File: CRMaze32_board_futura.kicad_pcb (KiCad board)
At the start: 2 copper layers, 74 x 100 mm, 70 parts, among them J101 CONN_01X02, J102 CONN_01X02, P101 GYRO_ADXRS_2, P102 GYRO_ADXRS_1, P103 SERIAL, P104 ENC_1_IN, P105 ENC_1_POWER, P106 ENC_2_IN, P107 ENC_2_POWER, P108 MOTOR1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

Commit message: retoques y moificaciones
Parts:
- removed P101: GYRO_ADXRS_2, Pin_Headers:Pin_Header_Straight_1x05
- added J103: GYRO_ADXRS_2, Pin_Headers:Pin_Header_Straight_1x06, F.Cu at (128.0, 55.5)
- moved C115 13.2 mm to (160.2, 67.7)
- moved C114 7.94 mm to (160.0, 65.2)
- moved C106 7.93 mm to (117.2, 60.9), turned to 270 degrees
- moved C105 4.42 mm to (114.5, 60.9), turned to 270 degrees
- moved 10ohm101 3.94 mm to (123.7, 53.9), turned to 50 degrees
- moved SW101 3.34 mm to (113.5, 72.5)
- moved D108 2.96 mm to (116.3, 56.7), turned to 50 degrees
- moved D106 2.56 mm to (155.0, 56.4), turned to 130 degrees
- moved 10uH101 2.51 mm to (128.5, 52.0)
- moved P107 2.33 mm to (157.0, 82.5)
- moved P104 2.27 mm to (113.5, 82.5)
- moved P102 1.97 mm to (133.6, 55.5)
- moved P105 1.90 mm to (113.5, 106.5), turned to 180 degrees
- moved 2.8ohm101 1.84 mm to (114.7, 65.3)
- moved D112 1.55 mm to (151.5, 52.1), turned to 130 degrees
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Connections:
- U101 pad 36: M1_DIR -> M1_EN
- U101 pad 37: M1_EN -> M1_DIR

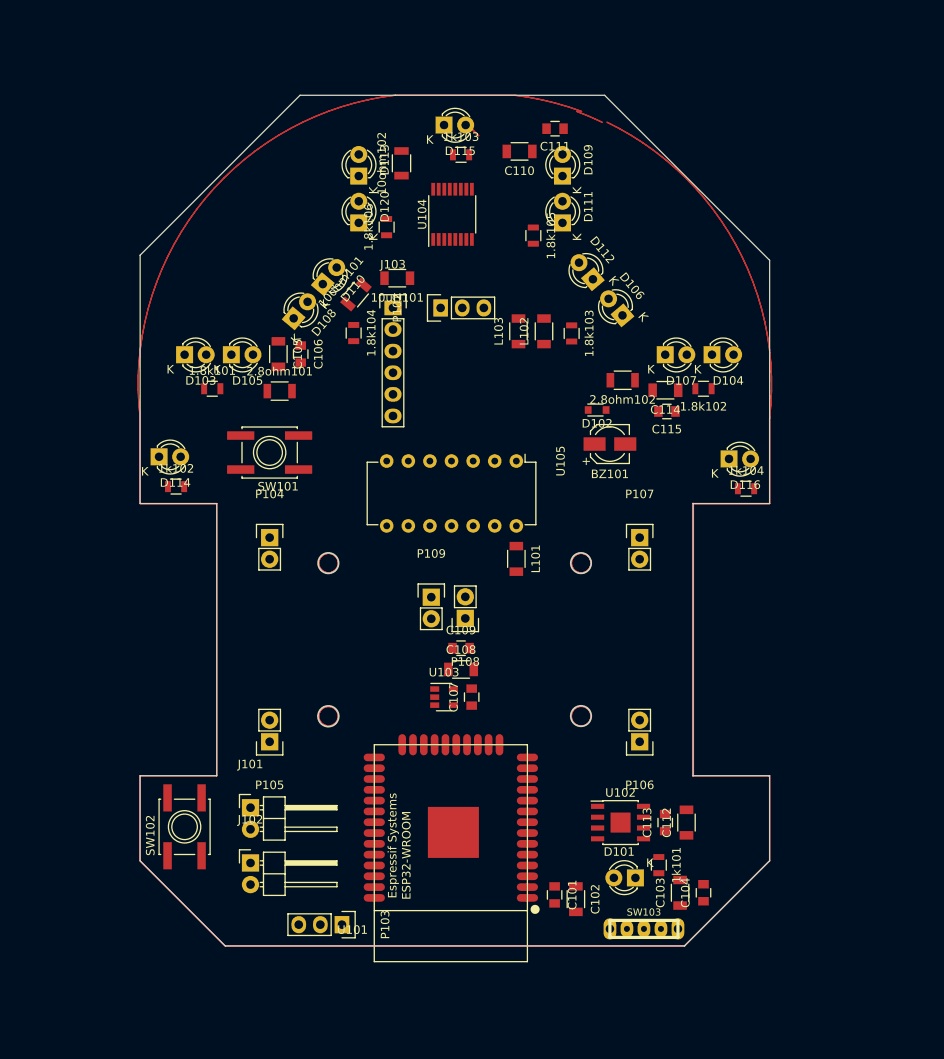
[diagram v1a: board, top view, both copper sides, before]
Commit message: esquematico finalizado. Componentes colocados. Comienzo del enrutado.
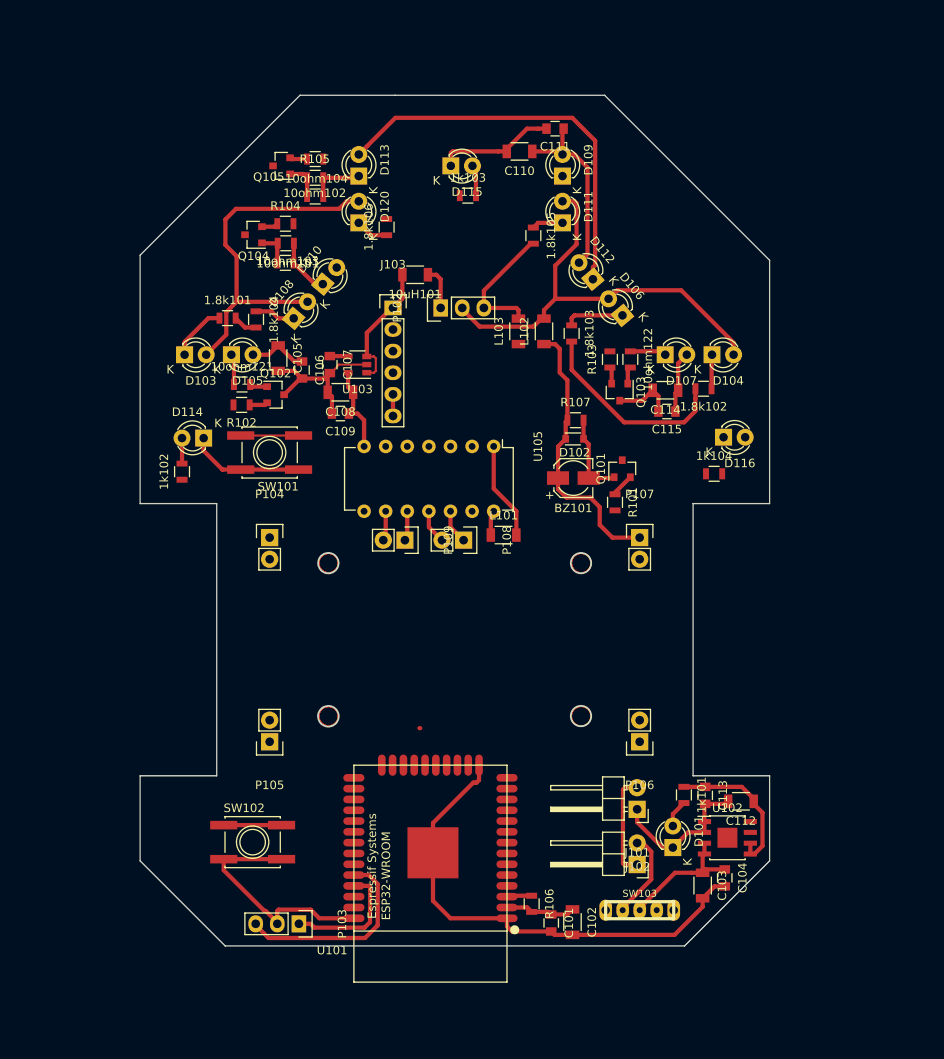
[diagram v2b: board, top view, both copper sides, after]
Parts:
- removed 2.8ohm101, 2.8ohm102: R, Resistors_SMD:R_1206
- removed U104: ULN2003A, Housings_SSOP:TSSOP-16_4.4x5mm_Pitch0.65mm
- added 10ohm103: R, Resistors_SMD:R_0805, F.Cu at (115.4, 47.9)
- added 10ohm104: R, Resistors_SMD:R_0805, F.Cu at (118.8, 40.2)
- added 10ohm121: R, Resistors_SMD:R_0805, F.Cu at (110.2, 64.5)
- added 10ohm122: R, Resistors_SMD:R_0805, F.Cu at (155.9, 61.5)
- added Q101: BS107, TO_SOT_Packages_SMD:SOT-23, F.Cu at (154.9, 74.4)
- added Q102: BS107, TO_SOT_Packages_SMD:SOT-23, F.Cu at (114.2, 65.7)
- added Q103: BS107, TO_SOT_Packages_SMD:SOT-23, F.Cu at (154.7, 65.4)
- added Q104: BS107, TO_SOT_Packages_SMD:SOT-23, F.Cu at (111.6, 46.9)
- added Q105: BS107, TO_SOT_Packages_SMD:SOT-23, F.Cu at (114.9, 38.8)
- added R101: R, Resistors_SMD:R_0805, F.Cu at (154.1, 78.3)
- added R102: R, Resistors_SMD:R_0805, F.Cu at (110.2, 66.9)
- added R103: R, Resistors_SMD:R_0805, F.Cu at (153.5, 61.5)
- added R104: R, Resistors_SMD:R_0805, F.Cu at (115.3, 45.6)
- added R105: R, Resistors_SMD:R_0805, F.Cu at (118.8, 38.0)
- added R106: R, Resistors_SMD:R_0805, F.Cu at (144.3, 125.5)
- added R107: R, Resistors_SMD:R_0805, F.Cu at (149.4, 68.7)
- 10ohm101, 10ohm102: footprint Resistors_SMD:R_1206 -> Resistors_SMD:R_0805
- moved J101 45.5 mm to (156.7, 114.4), turned to 180 degrees
- moved J102 45.5 mm to (156.7, 120.9), turned to 180 degrees
- moved C107 42.5 mm to (120.6, 62.2), turned to 270 degrees
- moved U103 40.4 mm to (123.8, 62.2), turned to 180 degrees
- moved C108 35.5 mm to (121.8, 65.4), turned to 180 degrees
- moved C109 31.0 mm to (121.8, 67.9), turned to 180 degrees
- moved U102 12.7 mm to (167.3, 117.8)
- moved 1.8k104 11.6 mm to (111.9, 56.9)
- moved 10ohm102 10.9 mm to (118.8, 42.4), turned to 180 degrees
- moved P108 9.20 mm to (136.3, 82.8), turned to 270 degrees
- moved 10ohm101 9.10 mm to (115.3, 50.2), turned to 180 degrees
- moved 1k101 8.76 mm to (162.2, 112.8)
- moved 1.8k101 8.49 mm to (108.5, 56.7)
- moved SW102 8.20 mm to (111.5, 118.3), turned to 0 degrees
- moved P109 7.38 mm to (129.4, 82.8), turned to 270 degrees
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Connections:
- net BUZZER_CONTROL renamed Net-(BZ101-Pad2)
- C104 pad 2: (no net) -> GND
- U101 pad 14: ENC_2_B -> M1_DIR
- U101 pad 29: GPIO_IR_SIDE -> M2_DIR
- U101 pad 31: M2_DIR -> GPIO_IR_SIDE
- U101 pad 37: M1_DIR -> ENC_2_B
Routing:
- net (no net): track 737.9 -> 50.3 mm
- net GND: track 0.00 -> 173.2 mm
- net VA3.3: track 0.00 -> 96.1 mm
- net 5V: track 0.00 -> 69.2 mm
- net V3.3: track 0.00 -> 51.3 mm
- net Net-(D112-Pad1): track 0.00 -> 47.1 mm
- net AGND: track 0.00 -> 41.8 mm
- net Net-(P103-Pad3): track 0.00 -> 23.8 mm
- net VBAT: track 0.00 -> 15.7 mm
- net Net-(P103-Pad1): track 0.00 -> 14.9 mm
- net Net-(J101-Pad2): track 0.00 -> 12.6 mm
- net Net-(J102-Pad2): track 0.00 -> 10.4 mm
- net Net-(BZ101-Pad2): track 0.00 -> 10.1 mm
- net Net-(R106-Pad1): track 0.00 -> 9.75 mm
- net IN_IR3: track 0.00 -> 6.96 mm
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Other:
- net class Finas added: clearance 0.2, trace_width 0.25, via_dia 0.6, via_drill 0.4
- net class Grandes added: clearance 0.4, trace_width 0.5, via_dia 0.8, via_drill 0.5

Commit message: avances enrutado
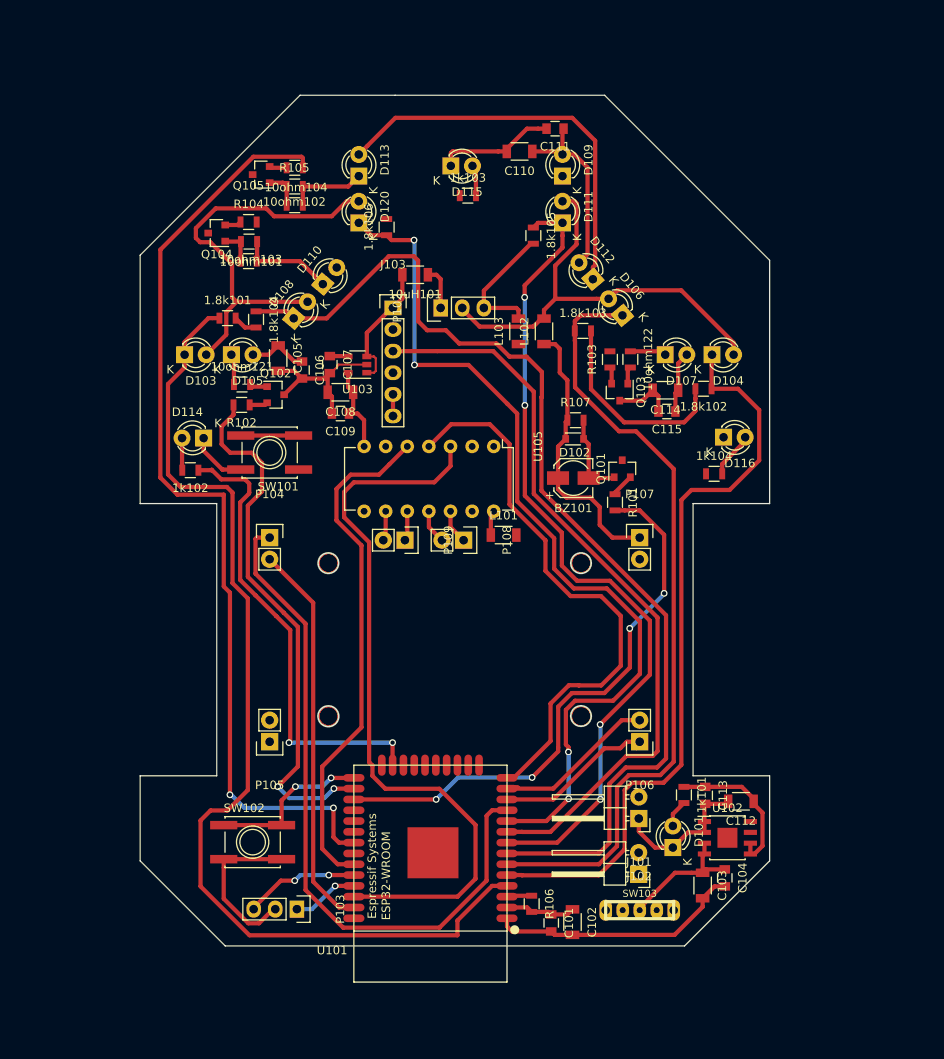
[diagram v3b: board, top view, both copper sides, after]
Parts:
- moved 10ohm103 4.33 mm to (111.1, 47.7)
- moved 10ohm101 4.33 mm to (111.0, 50.0)
- moved Q104 4.33 mm to (107.3, 46.7)
- moved R104 4.33 mm to (111.0, 45.4)
- moved Q105 2.61 mm to (112.5, 39.8)
- moved 10ohm102 2.61 mm to (116.5, 43.4)
- moved 10ohm104 2.61 mm to (116.5, 41.2)
- moved R105 2.61 mm to (116.5, 39.0)
- moved P103 1.74 mm to (116.7, 126.2)
- moved 1.8k103 1.36 mm to (150.3, 58.2), turned to 0 degrees
- moved J102 1.15 mm to (156.9, 122.1)
- moved J101 1.10 mm to (156.9, 115.5)
- moved 1k102 0.99 mm to (104.2, 74.6), turned to 180 degrees
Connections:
- U101 pad 12: ENC_1_B -> ENC_2_A
- U101 pad 13: ENC_2_A -> ENC_2_B
- U101 pad 37: ENC_2_B -> ENC_1_B
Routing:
- net IN_IR4: track 4.77 -> 125.7 mm
- net IN_IR1: track 6.76 -> 122.4 mm
- net GPIO_IR_SIDE: track 0.00 -> 112.1 mm, vias 0 -> 2
- net IN_IR6: track 3.88 -> 104.7 mm, vias 0 -> 4
- net IN_IR5: track 3.65 -> 97.2 mm, vias 0 -> 4
- net OUTZ: track 0.00 -> 88.4 mm
- net M1_EN: track 0.00 -> 86.8 mm
- net IN_IR3: track 6.96 -> 92.3 mm
- net IN_IR2: track 4.02 -> 88.8 mm
- net ENC_1_A: track 0.00 -> 81.1 mm
- net M1_DIR: track 0.00 -> 66.5 mm
- net GPIO_BUZZER: track 0.00 -> 66.2 mm, vias 0 -> 4
- net GPIO_IR_FL: track 0.00 -> 63.0 mm, vias 0 -> 2
- net M2_EN: track 0.00 -> 60.3 mm
- net GND: track 173.2 -> 117.5 mm
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
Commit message: pre cambio etiquetas esquematico
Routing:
- net M2_DIR: track 0.00 -> 61.5 mm, vias 0 -> 2
- net VBAT: track 15.7 -> 71.9 mm, vias 0 -> 2
- net GPIO_LED2: track 0.00 -> 20.9 mm
- net Net-(J101-Pad2): track 0.00 -> 11.3 mm
- net Net-(J102-Pad2): track 0.00 -> 8.96 mm
- net GND: track 117.5 -> 111.2 mm
- net GPIO_LED1: track 54.9 -> 53.9 mm
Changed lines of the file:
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@@
     (thickness 1.6)
     (drawings 25)
-    (tracks 1057)
+    (tracks 1098)
     (zones 0)
     (modules 83)
@@
     (35 F.Paste user hide)
     (36 B.SilkS user hide)
-    (37 F.SilkS user hide)
+    (37 F.SilkS user)
     (38 B.Mask user)
     (39 F.Mask user)
@@
   (segment (start 160.9 116.4) (end 160.9 115) (width 0.5) (layer F.Cu) (net 3))
   (segment (start 160.9 115) (end 162.2 113.7) (width 0.5) (layer F.Cu) (net 3))
-  (segment (start 127.95 106.6) (end 127.95 109.245) (width 0.5) (layer F.Cu) (net 4))
+  (segment (start 127.875 96.5) (end 127.875 109.17) (width 0.5) (layer F.Cu) (net 4))
+  (segment (start 127.875 109.17) (end 127.955 109.25) (width 0.5) (layer F.Cu) (net 4))
+  (segment (start 116.596201 95.75) (end 127.125 95.75) (width 0.5) (layer B.Cu) (net 4))
+  (segment (start 127.125 95.75) (end 127.875 96.5) (width 0.5) (layer B.Cu) (net 4))
+  (via (at 127.875 96.5) (size 0.8) (drill 0.5) (layers F.Cu B.Cu) (net 4))
+  (segment (start 115.771201 94.925) (end 116.596201 95.75) (width 0.5) (layer B.Cu) (net 4))
+  (segment (start 115.921191 93.368997) (end 115.921191 94.77501) (width 0.5) (layer F.Cu) (net 4))
+  (segment (start 115.921191 94.77501) (end 115.771201 94.925) (width 0.5) (layer F.Cu) (net 4))
+  (via (at 115.771201 94.925) (size 0.8) (drill 0.5) (layers F.Cu B.Cu) (net 4))
   (segment (start 127.95 109.245) (end 127.955 109.25) (width 0.5) (layer F.Cu) (net 4))
-  (segment (start 115.771201 106.6) (end 127.95 106.6) (width 0.5) (layer B.Cu) (net 4))
-  (via (at 127.95 106.6) (size 0.8) (drill 0.5) (layers F.Cu B.Cu) (net 4))
-  (segment (start 115.921191 93.368997) (end 115.921191 106.45001) (width 0.5) (layer F.Cu) (net 4))
-  (segment (start 115.921191 106.45001) (end 115.771201 106.6) (width 0.5) (layer F.Cu) (net 4))
-  (via (at 115.771201 106.6) (size 0.8) (drill 0.5) (layers F.Cu B.Cu) (net 4))
   (segment (start 111.833999 89.279611) (end 114.265991 91.711603) (width 0.5) (layer F.Cu) (net 4))
   (segment (start 114.265991 91.711603) (end 114.265992 91.713798) (width 0.5) (layer F.Cu) (net 4))
@@
   (segment (start 103.2 70.8) (end 103.2 74.55) (width 0.5) (layer F.Cu) (net 5))
   (segment (start 103.2 74.55) (end 103.225 74.575) (width 0.5) (layer F.Cu) (net 5))
+  (segment (start 126.094009 106.909009) (end 126.094009 88.6) (width 0.5) (layer F.Cu) (net 6))
+  (segment (start 126.685 109.25) (end 126.685 107.5) (width 0.5) (layer F.Cu) (net 6))
+  (segment (start 126.685 107.5) (end 126.094009 106.909009) (width 0.5) (layer F.Cu) (net 6))
   (segment (start 137.75 42.3) (end 137.75 39.21) (width 0.5) (layer F.Cu) (net 7))
   (segment (start 137.75 39.21) (end 137.34 38.8) (width 0.5) (layer F.Cu) (net 7))
@@
   (segment (start 147.4 75.5) (end 147.4 71.8) (width 0.5) (layer F.Cu) (net 15))
   (segment (start 147.4 71.8) (end 148.3 70.9) (width 0.5) (layer F.Cu) (net 15))
-  (segment (start 156.9 115.525) (end 156.9 117.041) (width 0.5) (layer F.Cu) (net 16))
-  (segment (start 156.9 117.041) (end 158.799 118.94) (width 0.5) (layer F.Cu) (net 16))
-  (segment (start 158.799 118.94) (end 159.684 118.94) (width 0.5) (layer F.Cu) (net 16))
   (segment (start 114.16 126.175) (end 113.912967 126.175) (width 0.5) (layer F.Cu) (net 16))
   (segment (start 113.912967 126.175) (end 112.246957 127.84101) (width 0.5) (layer F.Cu) (net 16))
@@
   (segment (start 161.1 129.2) (end 164.4 125.9) (width 0.5) (layer F.Cu) (net 16))
   (segment (start 164.4 125.9) (end 164.4 124.9) (width 0.5) (layer F.Cu) (net 16))
-  (segment (start 159.684 118.94) (end 160.9 118.94) (width 0.5) (layer F.Cu) (net 16))
   (segment (start 114.9 120.3) (end 108.1 120.3) (width 0.5) (layer F.Cu) (net 16))
   (segment (start 105.74 70.8) (end 105.74 72.3) (width 0.5) (layer F.Cu) (net 16))
@@
   (segment (start 141.375 36.8) (end 143.75 34.425) (width 0.5) (layer F.Cu) (net 16))
   (segment (start 143.75 34.425) (end 145.05 34.425) (width 0.5) (layer F.Cu) (net 16))
+  (segment (start 154.8 123.225) (end 157 125.425) (width 0.5) (layer F.Cu) (net 17))
+  (segment (start 157 125.425) (end 157 126.3) (width 0.5) (layer F.Cu) (net 17))
+  (segment (start 153.575 122) (end 154.8 123.225) (width 0.5) (layer B.Cu) (net 17))
+  (via (at 154.8 123.225) (size 0.8) (drill 0.5) (layers F.Cu B.Cu) (net 17))
+  (segment (start 153.575 96.875) (end 153.575 122) (width 0.5) (layer B.Cu) (net 17))
+  (segment (start 141.479998 86.65) (end 143.35 86.65) (width 0.5) (layer F.Cu) (net 17))
+  (segment (start 143.35 86.65) (end 153.575 96.875) (width 0.5) (layer F.Cu) (net 17))
+  (via (at 153.575 96.875) (size 0.8) (drill 0.5) (layers F.Cu B.Cu) (net 17))
+  (segment (start 137.3 79.4) (end 138.349999 80.449999) (width 0.5) (layer F.Cu) (net 17))
+  (segment (start 138.349999 80.449999) (end 138.349999 83.520001) (width 0.5) (layer F.Cu) (net 17))
+  (segment (start 138.349999 83.520001) (end 141.479998 86.65) (width 0.5) (layer F.Cu) (net 17))
   (segment (start 157 126.3) (end 157 126.05) (width 0.5) (layer F.Cu) (net 17))
   (segment (start 157 126.05) (end 161.15 121.9) (width 0.5) (layer F.Cu) (net 17))
@@
   (segment (start 124.293989 104.806011) (end 124.293989 83.416795) (width 0.5) (layer F.Cu) (net 37))
   (segment (start 124.293989 83.416795) (end 121.353988 80.476794) (width 0.5) (layer F.Cu) (net 37))
+  (segment (start 128.625 115.85) (end 123.43 115.85) (width 0.5) (layer F.Cu) (net 38))
+  (segment (start 123.43 115.85) (end 123.4 115.82) (width 0.5) (layer F.Cu) (net 38))
+  (segment (start 129.55 104.75) (end 129.55 114.925) (width 0.5) (layer B.Cu) (net 38))
+  (segment (start 129.55 114.925) (end 128.625 115.85) (width 0.5) (layer B.Cu) (net 38))
+  (via (at 128.625 115.85) (size 0.8) (drill 0.5) (layers F.Cu B.Cu) (net 38))
+  (segment (start 128.675 103.875) (end 129.55 104.75) (width 0.5) (layer B.Cu) (net 38))
+  (segment (start 127.65 103.875) (end 128.675 103.875) (width 0.5) (layer B.Cu) (net 38))
+  (segment (start 124.475 103.875) (end 127.65 103.875) (width 0.5) (layer B.Cu) (net 38))
+  (segment (start 123.243989 103.875) (end 124.475 103.875) (width 0.5) (layer B.Cu) (net 38))
+  (segment (start 123.393979 83.789591) (end 123.393979 103.72501) (width 0.5) (layer F.Cu) (net 38))
+  (segment (start 123.393979 103.72501) (end 123.243989 103.875) (width 0.5) (layer F.Cu) (net 38))
+  (via (at 123.243989 103.875) (size 0.8) (drill 0.5) (layers F.Cu B.Cu) (net 38))
+  (segment (start 127.14 71.78) (end 127.14 73.035) (width 0.5) (layer F.Cu) (net 38))
+  (segment (start 127.14 73.035) (end 125.97502 74.19998) (width 0.5) (layer F.Cu) (net 38))
+  (segment (start 125.97502 74.19998) (end 122.654407 74.199981) (width 0.5) (layer F.Cu) (net 38))
+  (segment (start 122.654407 74.199981) (end 120.45398 76.40041) (width 0.5) (layer F.Cu) (net 38))
+  (segment (start 120.45398 76.40041) (end 120.453979 80.849591) (width 0.5) (layer F.Cu) (net 38))
+  (segment (start 120.453979 80.849591) (end 123.393979 83.789591) (width 0.5) (layer F.Cu) (net 38))
   (segment (start 117.4 39.025) (end 117.4 37.875) (width 0.5) (layer F.Cu) (net 40))
   (segment (start 100.64999 75.442798) (end 102.657213 77.450021) (width 0.5) (layer F.Cu) (net 40))
@@
   (segment (start 121.06 112.01) (end 121.05 112) (width 0.5) (layer F.Cu) (net 43))
   (via (at 121.05 112) (size 0.8) (drill 0.5) (layers F.Cu B.Cu) (net 43))
+  (segment (start 156.875 122.075) (end 156.875 122.000682) (width 0.5) (layer F.Cu) (net 44))
+  (segment (start 156.875 122.000682) (end 158.566001 120.309681) (width 0.5) (layer F.Cu) (net 44))
+  (segment (start 158.566001 120.309681) (end 158.566001 113.214161) (width 0.5) (layer F.Cu) (net 44))
+  (segment (start 158.566001 113.214161) (end 158.33684 112.985) (width 0.5) (layer F.Cu) (net 44))
+  (segment (start 158.33684 112.985) (end 156.9 112.985) (width 0.5) (layer F.Cu) (net 44))
+  (segment (start 155 126.3) (end 155 124.979002) (width 0.5) (layer F.Cu) (net 45))
+  (segment (start 155 124.979002) (end 153.749999 123.729001) (width 0.5) (layer F.Cu) (net 45))
+  (segment (start 153.749999 123.729001) (end 153.749999 121.997999) (width 0.5) (layer F.Cu) (net 45))
+  (segment (start 153.749999 121.997999) (end 156.212998 119.535) (width 0.5) (layer F.Cu) (net 45))
+  (segment (start 156.212998 119.535) (end 156.875 119.535) (width 0.5) (layer F.Cu) (net 45))
   (segment (start 148.625 107.7) (end 148.625 107.134315) (width 0.5) (layer F.Cu) (net 46))
   (segment (start 153.127204 88.47501) (end 149.254761 88.475009) (width 0.5) (layer F.Cu) (net 46))
